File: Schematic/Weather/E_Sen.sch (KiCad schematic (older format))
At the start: 27 parts, among them J23 3_Way_Wire, J24 3_Way_Wire, Q7 AO3401, Q8 AO3401, Q9 BSS138, U6 LM321

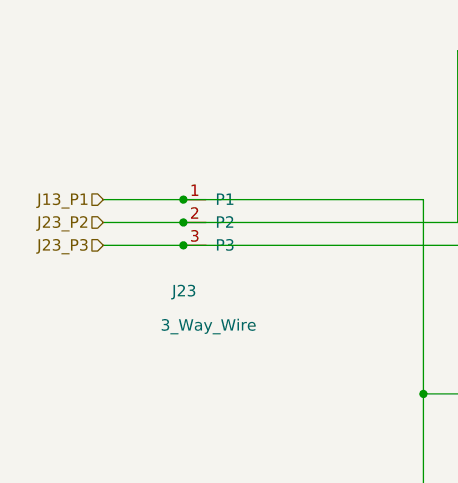
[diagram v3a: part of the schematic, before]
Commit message: config connectors sda scl
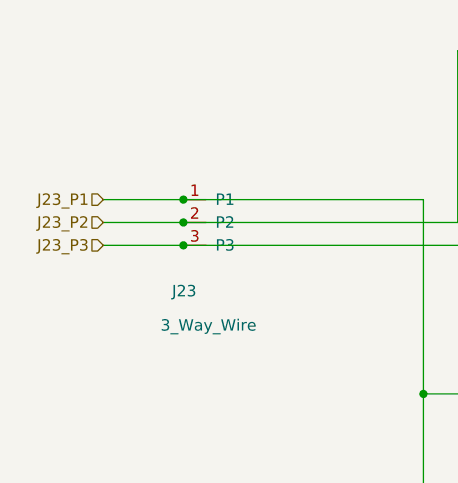
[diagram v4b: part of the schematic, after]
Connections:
- net J13_P1 renamed J23_P1
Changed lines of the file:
@@
 Comment4 ""
 $EndDescr
-Text HLabel 3200 1950 0    50   Input ~ 0
-J13_P1
-Text HLabel 3200 2050 0    50   Input ~ 0
-J23_P2
-Text HLabel 3200 2150 0    50   Input ~ 0
-J23_P3
-Text HLabel 3200 3400 0    50   Input ~ 0
-J24_P2
 $Comp
 L Weather-rescue:AO3401-Transistor_FET Q?
@@
 	6300 4250 6300 4550
 Wire Wire Line
-	5750 3400 6100 3400
-Wire Wire Line
 	5750 3500 5750 3400
 Wire Wire Line
@@
 	6350 2450 6350 2200
 Connection ~ 6350 2200
-Text HLabel 3200 3500 0    50   Input ~ 0
-J24_P3
 Wire Wire Line
 	5750 3800 5750 3900
@@
 Wire Wire Line
 	4750 1300 6150 1300
-$Comp
-L MyComponents:3_Way_Wire J?
-U 1 1 5CAEF15D
-P 3650 1950
-AR Path="/5C952539/5CAEF15D" Ref="J?"  Part="1"
-AR Path="/5CAC04D1/5CAEF15D" Ref="J23"  Part="1"
-F 0 "J23" H 3500 1550 50  0000 L CNN
-F 1 "3_Way_Wire" H 3450 1400 50  0000 L CNN
-F 2 "Connector_PinHeader_2.54mm:PinHeader_1x03_P2.54mm_Vertical" H 3650 1950 50  0001 C CNN
-F 3 "" H 3650 1950 50  0001 C CNN
-	1    3650 1950
-	1    0    0    -1
-$EndComp
 Wire Wire Line
 	4600 1950 4600 2800
-Wire Wire Line
-	3200 1950 3550 1950
-Connection ~ 3550 1950
-Wire Wire Line
-	3550 1950 4600 1950
 Connection ~ 4600 2800
-$Comp
-L MyComponents:3_Way_Wire J?
-U 1 1 5CAEF168
-P 3600 3300
-AR Path="/5C952539/5CAEF168" Ref="J?"  Part="1"
-AR Path="/5CAC04D1/5CAEF168" Ref="J24"  Part="1"
-F 0 "J24" H 3500 2900 50  0000 L CNN
-F 1 "3_Way_Wire" H 3450 2750 50  0000 L CNN
-F 2 "Connector_PinHeader_2.54mm:PinHeader_1x03_P2.54mm_Vertical" H 3600 3300 50  0001 C CNN
-F 3 "" H 3600 3300 50  0001 C CNN
-	1    3600 3300
-	1    0    0    -1
-$EndComp
-Wire Wire Line
-	3500 3300 4600 3300
 Connection ~ 4600 3300
 Wire Wire Line
@@
 	4750 2050 4750 1300
 Wire Wire Line
-	3200 2050 3550 2050
-Connection ~ 3550 2050
-Wire Wire Line
-	3550 2050 4750 2050
-Wire Wire Line
 	4900 2100 4900 2150
 Wire Wire Line
-	4900 2150 3550 2150
-Wire Wire Line
-	3200 2150 3550 2150
-Connection ~ 3550 2150
-Wire Wire Line
-	3200 3500 3500 3500
-Wire Wire Line
-	3500 3500 5300 3500
-Wire Wire Line
 	5300 3500 5300 4750
-Connection ~ 3500 3500
-Wire Wire Line
-	3200 3400 3500 3400
-Wire Wire Line
-	3500 3400 5750 3400
-Connection ~ 3500 3400
 Connection ~ 5750 3400
 $Comp
@@
 Wire Wire Line
 	7950 3900 8350 3900
+Wire Wire Line
+	5750 3400 6100 3400
+Connection ~ 3500 3400
+Wire Wire Line
+	3500 3400 5750 3400
+Wire Wire Line
+	3200 3400 3500 3400
+Connection ~ 3500 3500
+Wire Wire Line
+	3500 3500 5300 3500
+Wire Wire Line
+	3200 3500 3500 3500
+Connection ~ 3550 2150
+Wire Wire Line
+	3200 2150 3550 2150
+Wire Wire Line
+	4900 2150 3550 2150
+Wire Wire Line
+	3550 2050 4750 2050
+Connection ~ 3550 2050
+Wire Wire Line
+	3200 2050 3550 2050
+Wire Wire Line
+	3500 3300 4600 3300
+$Comp
+L MyComponents:3_Way_Wire J?
+U 1 1 5CAEF168
+P 3600 3300
+AR Path="/5C952539/5CAEF168" Ref="J?"  Part="1"
+AR Path="/5CAC04D1/5CAEF168" Ref="J24"  Part="1"
+F 0 "J24" H 3500 2900 50  0000 L CNN
+F 1 "3_Way_Wire" H 3450 2750 50  0000 L CNN
+F 2 "Connector_PinHeader_2.54mm:PinHeader_1x03_P2.54mm_Vertical" H 3600 3300 50  0001 C CNN
+F 3 "" H 3600 3300 50  0001 C CNN
+	1    3600 3300
+	1    0    0    -1
+$EndComp
+Wire Wire Line
+	3550 1950 4600 1950
+Connection ~ 3550 1950
+Wire Wire Line
+	3200 1950 3550 1950
+$Comp
+L MyComponents:3_Way_Wire J?
+U 1 1 5CAEF15D
+P 3650 1950
+AR Path="/5C952539/5CAEF15D" Ref="J?"  Part="1"
+AR Path="/5CAC04D1/5CAEF15D" Ref="J23"  Part="1"
+F 0 "J23" H 3500 1550 50  0000 L CNN
+F 1 "3_Way_Wire" H 3450 1400 50  0000 L CNN
+F 2 "Connector_PinHeader_2.54mm:PinHeader_1x03_P2.54mm_Vertical" H 3650 1950 50  0001 C CNN
+F 3 "" H 3650 1950 50  0001 C CNN
+	1    3650 1950
+	1    0    0    -1
+$EndComp
+Text HLabel 3200 3500 0    50   Input ~ 0
+J24_P3
+Text HLabel 3200 3400 0    50   Input ~ 0
+J24_P2
+Text HLabel 3200 2150 0    50   Input ~ 0
+J23_P3
+Text HLabel 3200 2050 0    50   Input ~ 0
+J23_P2
+Text HLabel 3200 1950 0    50   Input ~ 0
+J23_P1
 $EndSCHEMATC
